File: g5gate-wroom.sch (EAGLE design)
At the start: 28 parts, among them IC1 TCAN1051HGV, U2 XN04312, U8 NCP1117LPST50T3G

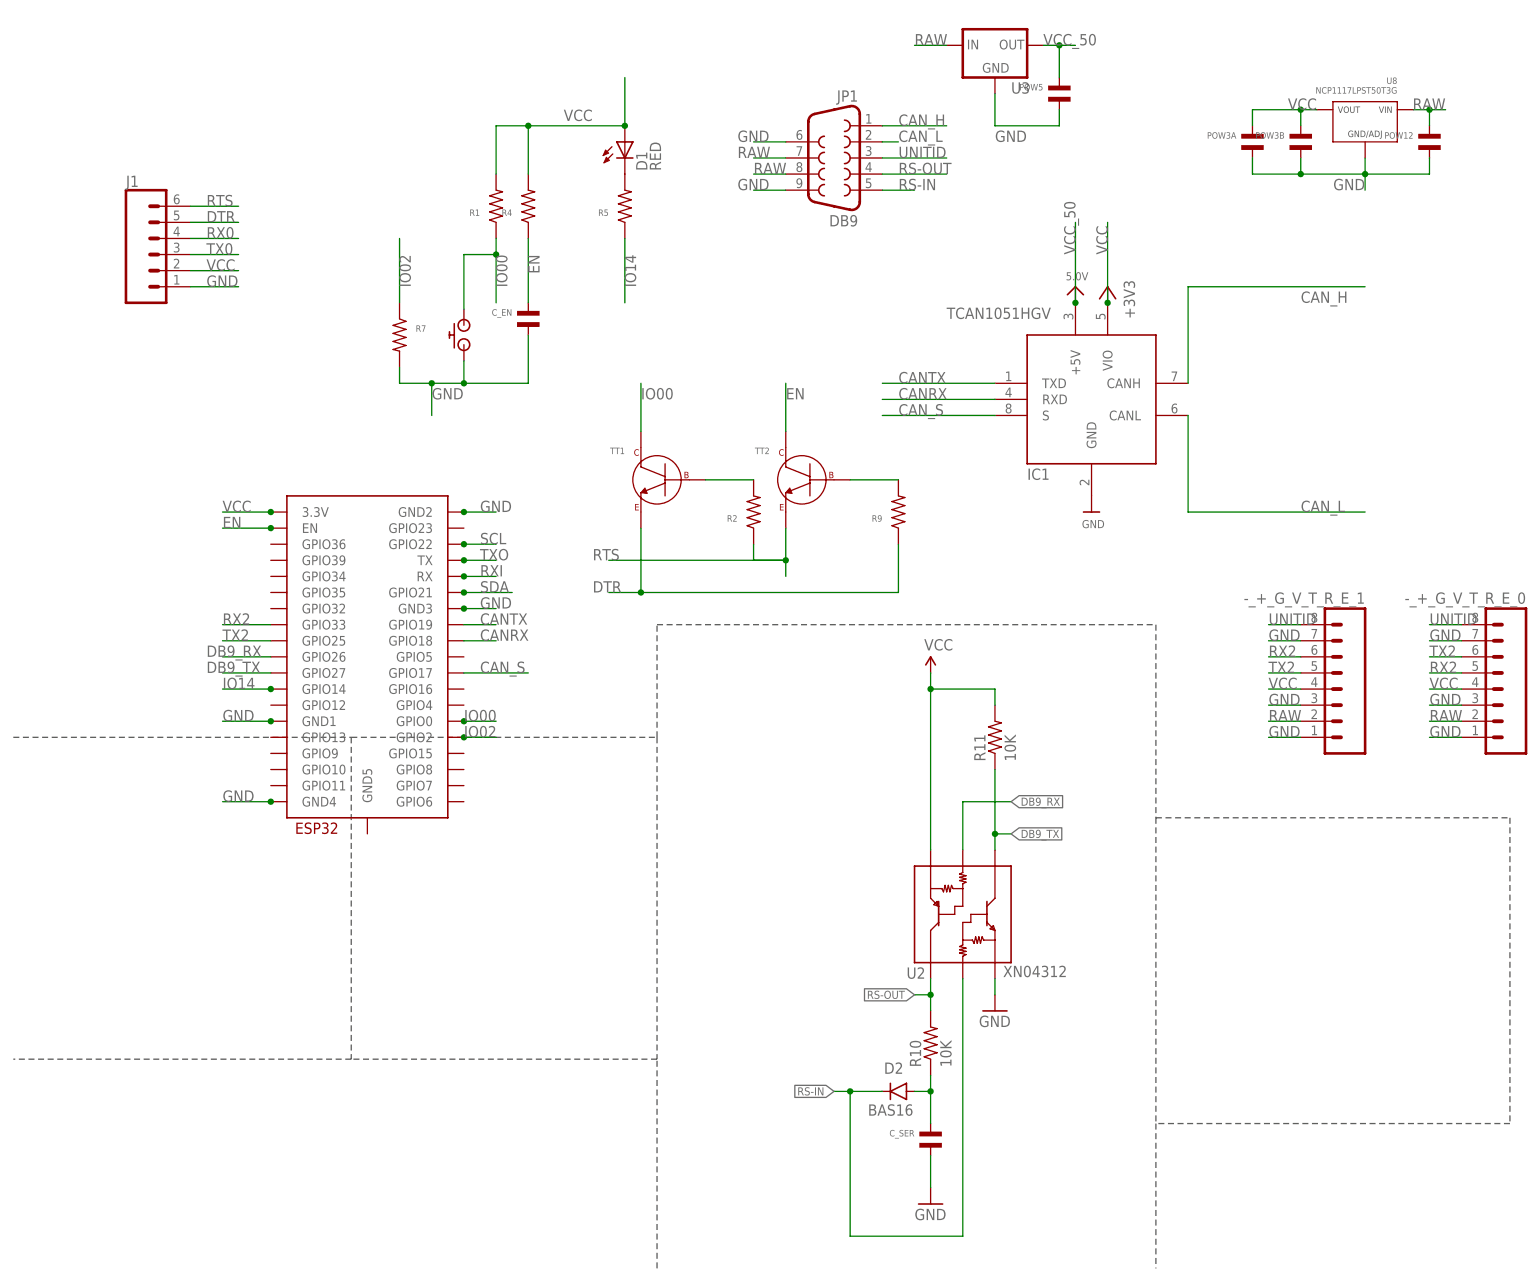
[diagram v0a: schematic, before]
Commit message: Add touchscreen header directly to board
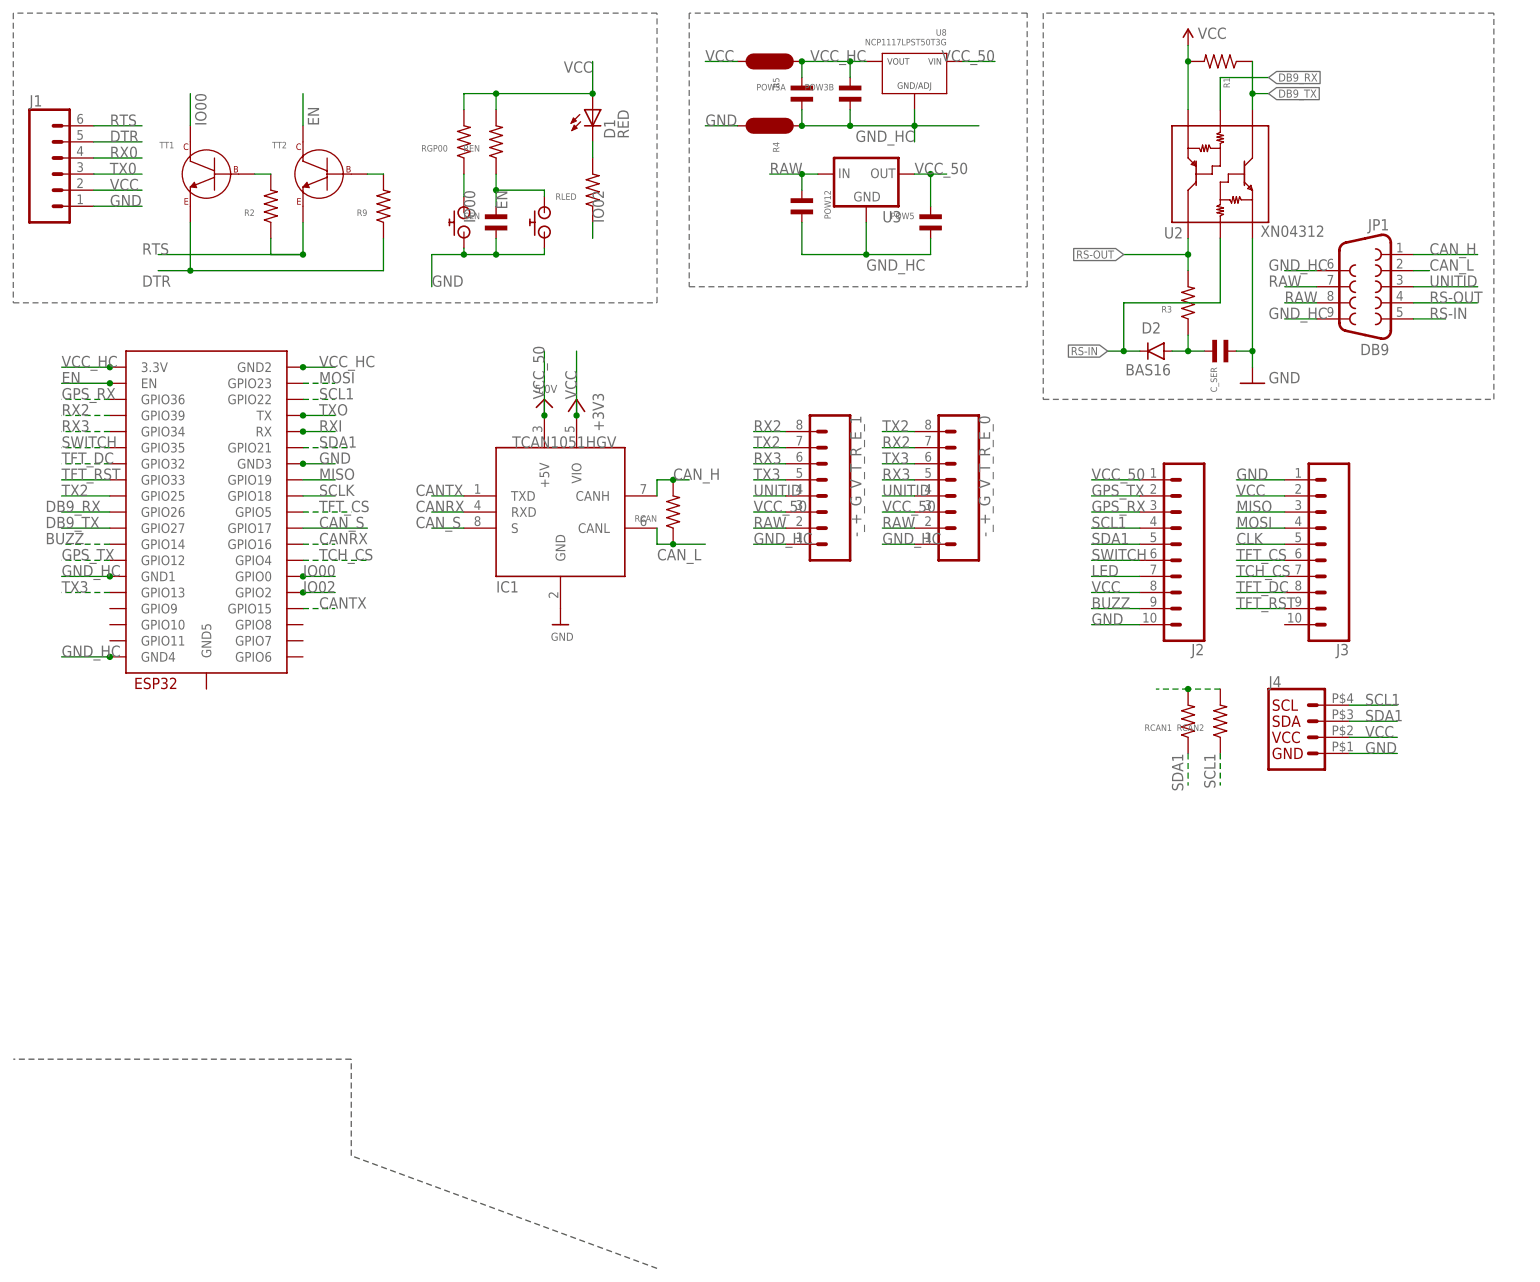
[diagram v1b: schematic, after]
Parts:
- removed C_EN: (no value), MF_Passives:CAPACITOR_NP_0603
- removed R10, R11: 10K, SparkFun-Resistors:10KOHM1/10W1%(0603)0603
- removed R7: (no value), 00jim:RESISTOR_0603
- added CEN: (no value), MF_Passives:CAPACITOR_NP_0603
- added J2, J3: (no value), SparkFun-Connectors:CONN_10
- added J4: Vertical Qwiic Connector, 00jim:QWIIC_CONNECTORJST04_1MM_HOLE
- added R3, RCAN, RCAN1, RCAN2, REN, RGP00, RLED: (no value), 00jim:RESISTOR_0603
- added U$2: AMAZON_BUTTONB2010, 00jim:AMAZON_BUTTONB2010
- R4, R5: device 00jim:RESISTOR_0603 -> 00jim:JUMPER
- U$1: value AMAZON_BUTTON -> AMAZON_BUTTONB2010; device 00jim:AMAZON_BUTTON -> 00jim:AMAZON_BUTTONB2010
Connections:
- removed net IO14: R5.P$1, U$3.GPIO14
- removed net SCL: U$3.GPIO22
- removed net SDA: U$3.GPIO21
- new net BUZZ: J2.9, U$3.GPIO14
- new net CLK: J3.5
- new net GND_HC: -_+_G_V_T_R_E_0.1, -_+_G_V_T_R_E_1.1, JP1.6, JP1.9, POW12.P$2, POW3A.P$2, POW3B.P$2, POW5.P$2, R4.P$1, U$3.GND1, U$3.GND4, U3.GND, U8.GND/ADJ
- new net GPS_RX: J2.3, U$3.GPIO36
- new net GPS_TX: J2.2, U$3.GPIO12
- new net LED: J2.7
- new net MISO: J3.3, U$3.GPIO19
- new net MOSI: J3.4, U$3.GPIO23
- new net RX3: -_+_G_V_T_R_E_0.5, -_+_G_V_T_R_E_1.6, U$3.GPIO34
- new net SCL1: J2.4, J4.4, RCAN2.P$1, U$3.GPIO22
- new net SCLK: U$3.GPIO18
- new net SDA1: J2.5, J4.3, RCAN1.P$1, U$3.GPIO21
- new net SWITCH: J2.6, U$3.GPIO35
- new net TCH_CS: J3.7, U$3.GPIO4
- new net TFT_CS: J3.6, U$3.GPIO5
- new net TFT_DC: J3.8, U$3.GPIO32
- new net TFT_RST: J3.9, U$3.GPIO33
- new net TX3: -_+_G_V_T_R_E_0.6, -_+_G_V_T_R_E_1.5, U$3.GPIO13
- new net VCC_HC: POW3A.P$1, POW3B.P$1, R5.P$1, U$3.3.3V, U$3.GND2, U8.VOUT
- net CANRX: now also U$3.GPIO16; no longer U$3.GPIO18
- net CANTX: now also U$3.GPIO15; no longer U$3.GPIO19
- net CAN_H: now also RCAN.P$2
- net CAN_L: now also RCAN.P$1
- net DB9_TX: now also R1.P$1; no longer R11.1
- net EN: now also CEN.P$1, REN.P$1, U$2.P$1; no longer C_EN.P$1, R4.P$1
- net GND: now also CEN.P$2, J2.10, J3.1, J4.1, R4.P$2, U$2.P$2; no longer -_+_G_V_T_R_E_0.1, -_+_G_V_T_R_E_0.3, -_+_G_V_T_R_E_0.7, -_+_G_V_T_R_E_1.1, -_+_G_V_T_R_E_1.3, -_+_G_V_T_R_E_1.7, C_EN.P$2, JP1.6, JP1.9, POW12.P$2, POW3A.P$2, POW3B.P$2, POW5.P$2, R7.P$2, U$3.GND1, U$3.GND2, U$3.GND4, U3.GND, U8.GND/ADJ
- net IO00: now also RGP00.P$1; no longer R1.P$1
- net IO02: now also RLED.P$1; no longer R7.P$1
- net N$2: now also RLED.P$2; no longer R5.P$2
- net N$4: now also R3.P$1; no longer R10.1
- net RAW: no longer U8.VIN
- net RS-OUT: now also R3.P$2; no longer R10.2
- net RX2: now also -_+_G_V_T_R_E_0.7, -_+_G_V_T_R_E_1.8, U$3.GPIO39; no longer -_+_G_V_T_R_E_0.5, -_+_G_V_T_R_E_1.6, U$3.GPIO33
- net TX2: now also -_+_G_V_T_R_E_0.8, -_+_G_V_T_R_E_1.7; no longer -_+_G_V_T_R_E_0.6, -_+_G_V_T_R_E_1.5
- net UNITID: now also -_+_G_V_T_R_E_0.4, -_+_G_V_T_R_E_1.4; no longer -_+_G_V_T_R_E_0.8, -_+_G_V_T_R_E_1.8
- net VCC: now also J2.8, J3.2, J4.2, R5.P$2, RCAN1.P$2, RCAN2.P$2, REN.P$2, RGP00.P$2; no longer -_+_G_V_T_R_E_0.4, -_+_G_V_T_R_E_1.4, POW3A.P$1, POW3B.P$1, R11.2, R4.P$2, U$3.3.3V, U8.VOUT
- net VCC_50: now also -_+_G_V_T_R_E_0.3, -_+_G_V_T_R_E_1.3, J2.1, U8.VIN
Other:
- moved on the sheet: -_+_G_V_T_R_E_0, -_+_G_V_T_R_E_1, C_SER, D1, D2, IC1, J1, JP1, POW12, POW3A, POW3B, POW5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

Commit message: wroom test two sided
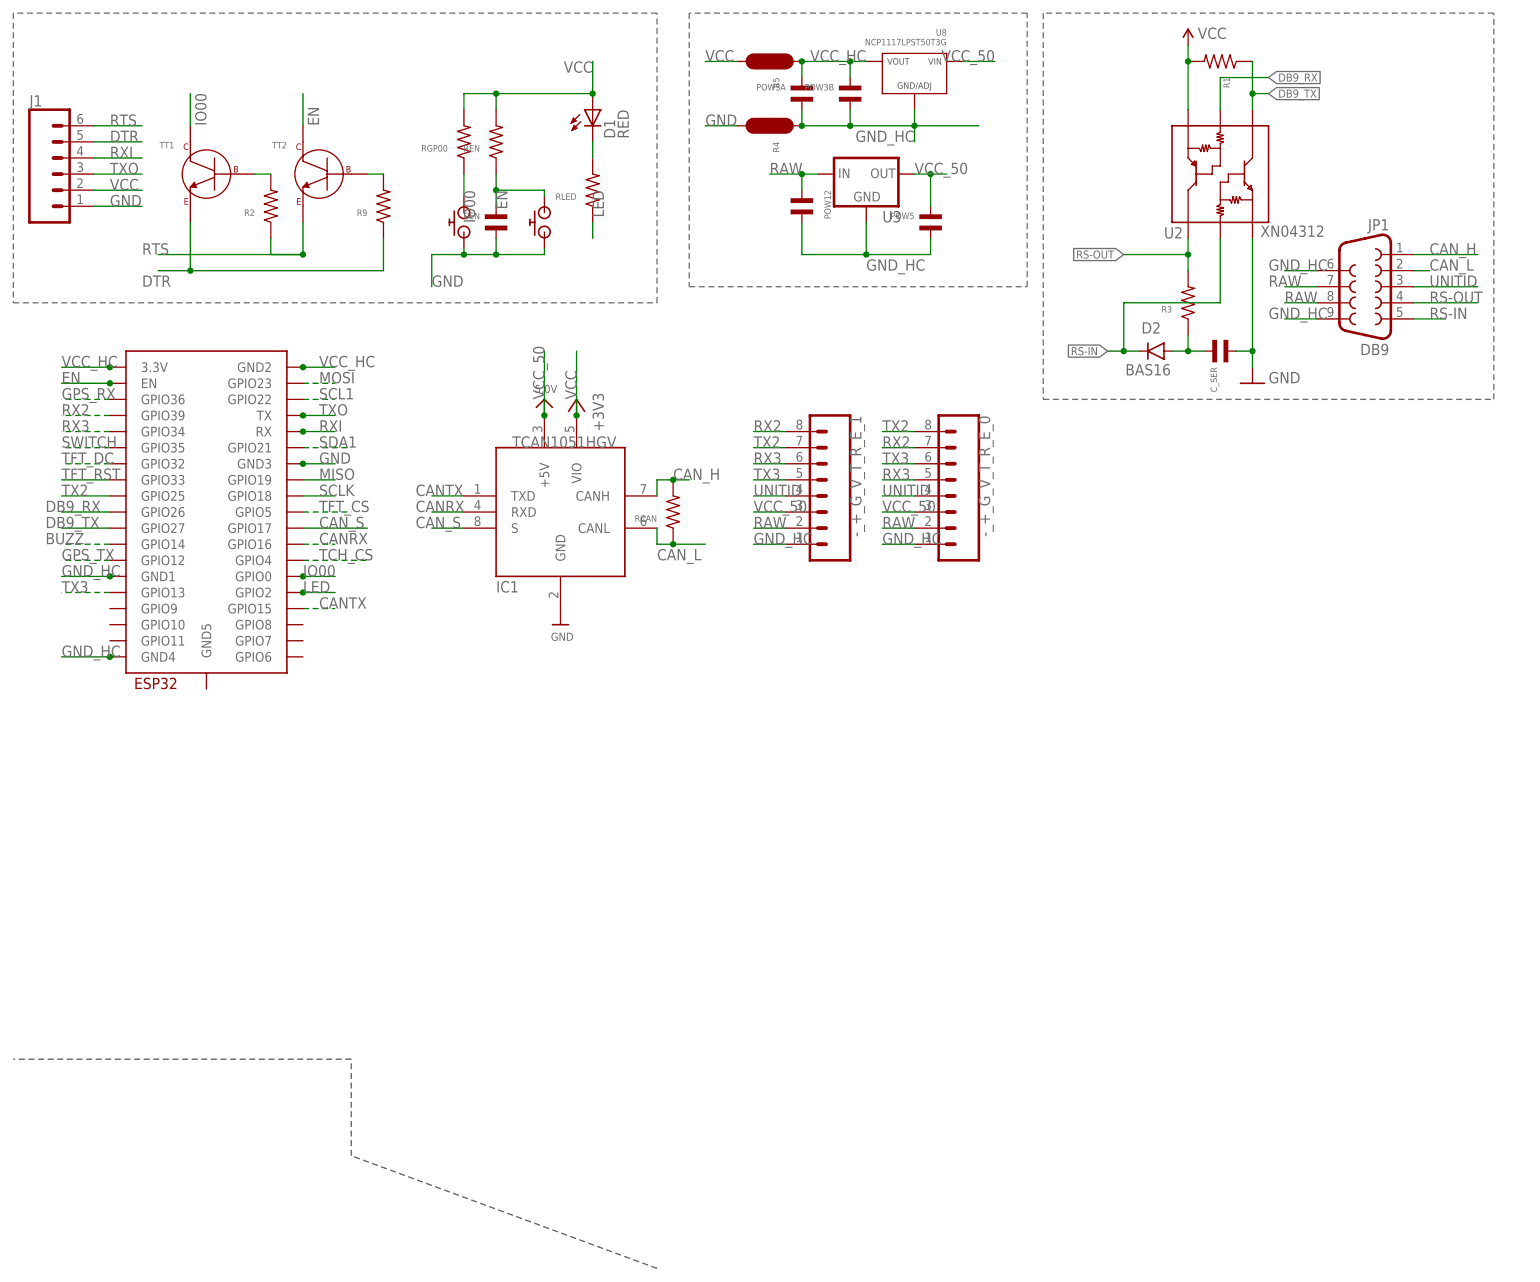
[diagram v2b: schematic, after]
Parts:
- removed J2, J3: (no value), SparkFun-Connectors:CONN_10
- removed J4: Vertical Qwiic Connector, 00jim:QWIIC_CONNECTORJST04_1MM_HOLE
- removed RCAN1, RCAN2: (no value), 00jim:RESISTOR_0603
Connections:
- removed net CLK: J3.5
- removed net IO02: RLED.P$1, U$3.GPIO2
- removed net RX0: J1.4
- removed net TX0: J1.3
- net BUZZ: no longer J2.9
- net GND: no longer J2.10, J3.1, J4.1
- net GPS_RX: no longer J2.3
- net GPS_TX: no longer J2.2
- net LED: now also RLED.P$1, U$3.GPIO2; no longer J2.7
- net MISO: no longer J3.3
- net MOSI: no longer J3.4
- net RXI: now also J1.4
- net SCL1: no longer J2.4, J4.4, RCAN2.P$1
- net SDA1: no longer J2.5, J4.3, RCAN1.P$1
- net SWITCH: no longer J2.6
- net TCH_CS: no longer J3.7
- net TFT_CS: no longer J3.6
- net TFT_DC: no longer J3.8
- net TFT_RST: no longer J3.9
- net TXO: now also J1.3
- net VCC: no longer J2.8, J3.2, J4.2, RCAN1.P$2, RCAN2.P$2
- net VCC_50: no longer J2.1
